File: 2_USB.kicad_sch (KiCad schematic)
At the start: 11 parts, among them J301 USB_C_Receptacle_USB2.0_16P, J302 Conn_01x03, J303 Conn_01x03, U301 CH224K, U302 FSUSB42MUX

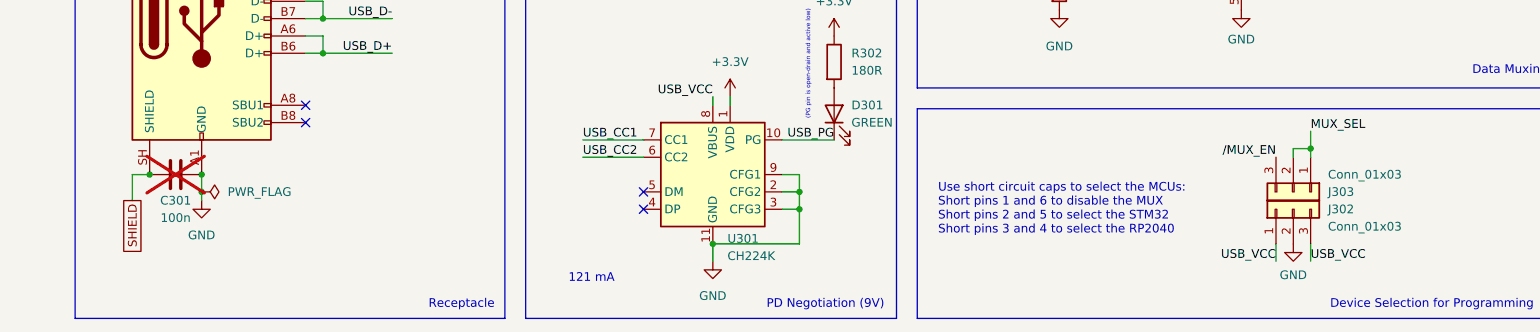
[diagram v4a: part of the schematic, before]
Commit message: Renamed a few nets
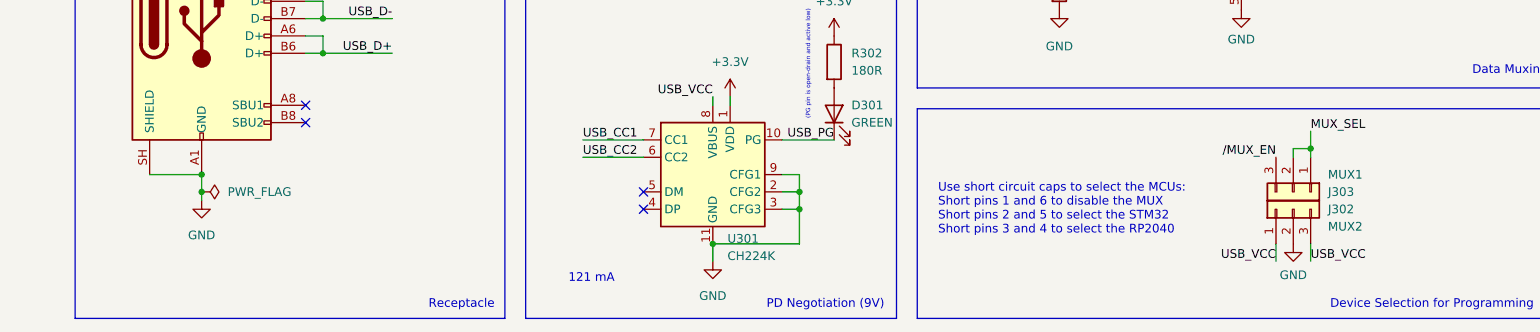
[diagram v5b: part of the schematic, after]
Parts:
- removed C301: 100n, Capacitor_SMD:C_0603_1608Metric, symbol Device:C
- J302: value Conn_01x03 -> MUX2
- J303: value Conn_01x03 -> MUX1
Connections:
- net SHIELD is gone; now on net GND: J301.SH (SHIELD)
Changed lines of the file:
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@@
 	)
 	(junction
-		(at 49.53 125.73)
+		(at 87.63 85.09)
+		(diameter 0)
+		(color 0 0 0 0)
+	)
+	(junction
+		(at 144.78 128.27)
 		(diameter 0)
 		(color 0 0 0 0)
@@
 	)
 	(junction
-		(at 87.63 85.09)
-		(diameter 0)
-		(color 0 0 0 0)
-	)
-	(junction
-		(at 144.78 128.27)
-		(diameter 0)
-		(color 0 0 0 0)
-	)
-	(junction
 		(at 85.09 85.09)
 		(diameter 0)
@@
 	(wire
 		(pts
-			(xy 46.99 129.54) (xy 46.99 125.73)
-		)
-		(stroke
-			(width 0)
-			(type default)
-		)
-	)
-	(wire
-		(pts
 			(xy 57.15 128.27) (xy 57.15 129.54)
 		)
@@
 	(wire
 		(pts
+			(xy 49.53 125.73) (xy 57.15 125.73)
+		)
+		(stroke
+			(width 0)
+			(type default)
+		)
+	)
+	(wire
+		(pts
 			(xy 132.08 114.3) (xy 132.08 115.57)
 		)
@@
 		(pts
 			(xy 144.78 128.27) (xy 144.78 130.81)
-		)
-		(stroke
-			(width 0)
-			(type default)
-		)
-	)
-	(wire
-		(pts
-			(xy 46.99 125.73) (xy 49.53 125.73)
 		)
 		(stroke
@@
 			)
 			(justify right bottom)
-		)
-	)
-	(global_label "SHIELD"
-		(shape passive)
-		(at 46.99 129.54 270)
-		(fields_autoplaced yes)
-		(effects
-			(font
-				(size 1.27 1.27)
-			)
-			(justify right)
-		)
-		(property "Intersheetrefs" "${INTERSHEET_REFS}"
-			(at 46.99 138.0058 90)
-			(hide yes)
-			(show_name no)
-			(do_not_autoplace no)
-			(effects
-				(font
-					(size 1.27 1.27)
-				)
-				(justify right)
-			)
 		)
 	)
@@
 			)
 		)
-		(property "Value" "Conn_01x03"
+		(property "Value" "MUX1"
 			(at 222.25 125.73 90)
 			(show_name no)
@@
 			)
 		)
-		(property "Value" "Conn_01x03"
+		(property "Value" "MUX2"
 			(at 222.25 133.35 90)
 			(show_name no)
@@
 					(unit 1)
 				)
-			)
-		)
-	)
-	(symbol
-		(lib_id "Device:C")
-		(at 53.34 125.73 90)
-		(unit 1)
-		(body_style 1)
-		(exclude_from_sim no)
-		(in_bom yes)
-		(on_board yes)
-		(in_pos_files yes)
-		(dnp yes)
-		(property "Reference" "C301"
-			(at 53.34 129.54 90)
-			(show_name no)
-			(do_not_autoplace no)
-			(effects
-				(font
-					(size 1.27 1.27)
-				)
-			)
-		)
-		(property "Value" "100n"
-			(at 53.34 132.08 90)
-			(show_name no)
-			(do_not_autoplace no)
-			(effects
-				(font
-					(size 1.27 1.27)
-				)
-			)
-		)
-		(property "Footprint" "Capacitor_SMD:C_0603_1608Metric"
-			(at 57.15 124.7648 0)
-			(hide yes)
-			(show_name no)
-			(do_not_autoplace no)
-			(effects
-				(font
-					(size 1.27 1.27)
-				)
-			)
-		)
-		(property "Datasheet" ""
-			(at 53.34 125.73 0)
-			(hide yes)
-			(show_name no)
-			(do_not_autoplace no)
-			(effects
-				(font
-					(size 1.27 1.27)
-				)
-			)
-		)
-		(property "Description" "Unpolarized capacitor"
-			(at 53.34 125.73 0)
-			(hide yes)
-			(show_name no)
-			(do_not_autoplace no)
-			(effects
-				(font
-					(size 1.27 1.27)
-				)
-			)
-		)
-		(property "LCSC Part Name" ""
-			(at 53.34 125.73 90)
-			(hide yes)
-			(show_name no)
-			(do_not_autoplace no)
-			(effects
-				(font
-					(size 1.27 1.27)
-				)
-			)
-		)
-		(property "Manufacturer Part" ""
-			(at 53.34 125.73 90)
-			(hide yes)
-			(show_name no)
-			(do_not_autoplace no)
-			(effects
-				(font
-					(size 1.27 1.27)
-				)
-			)
-		)
-		(property "Supplier" ""
-			(at 53.34 125.73 90)
-			(hide yes)
-			(show_name no)
-			(do_not_autoplace no)
-			(effects
-				(font
-					(size 1.27 1.27)
-				)
-			)
-		)
-		(property "Supplier Part" ""
-			(at 53.34 125.73 90)
-			(hide yes)
-			(show_name no)
-			(do_not_autoplace no)
-			(effects
-				(font
-					(size 1.27 1.27)
-				)
-			)
-		)
-		(pin "2"
-		)
-		(pin "1"
-		)
-		(instances
-			(project "polaris"
-				(path "/cfb90e19-9fbe-47a1-a5ac-df522853d1d0/f51c22fe-6c27-4a6e-b54b-9941150cfe5c"
-					(reference "C301")
-					(unit 1)
-				)

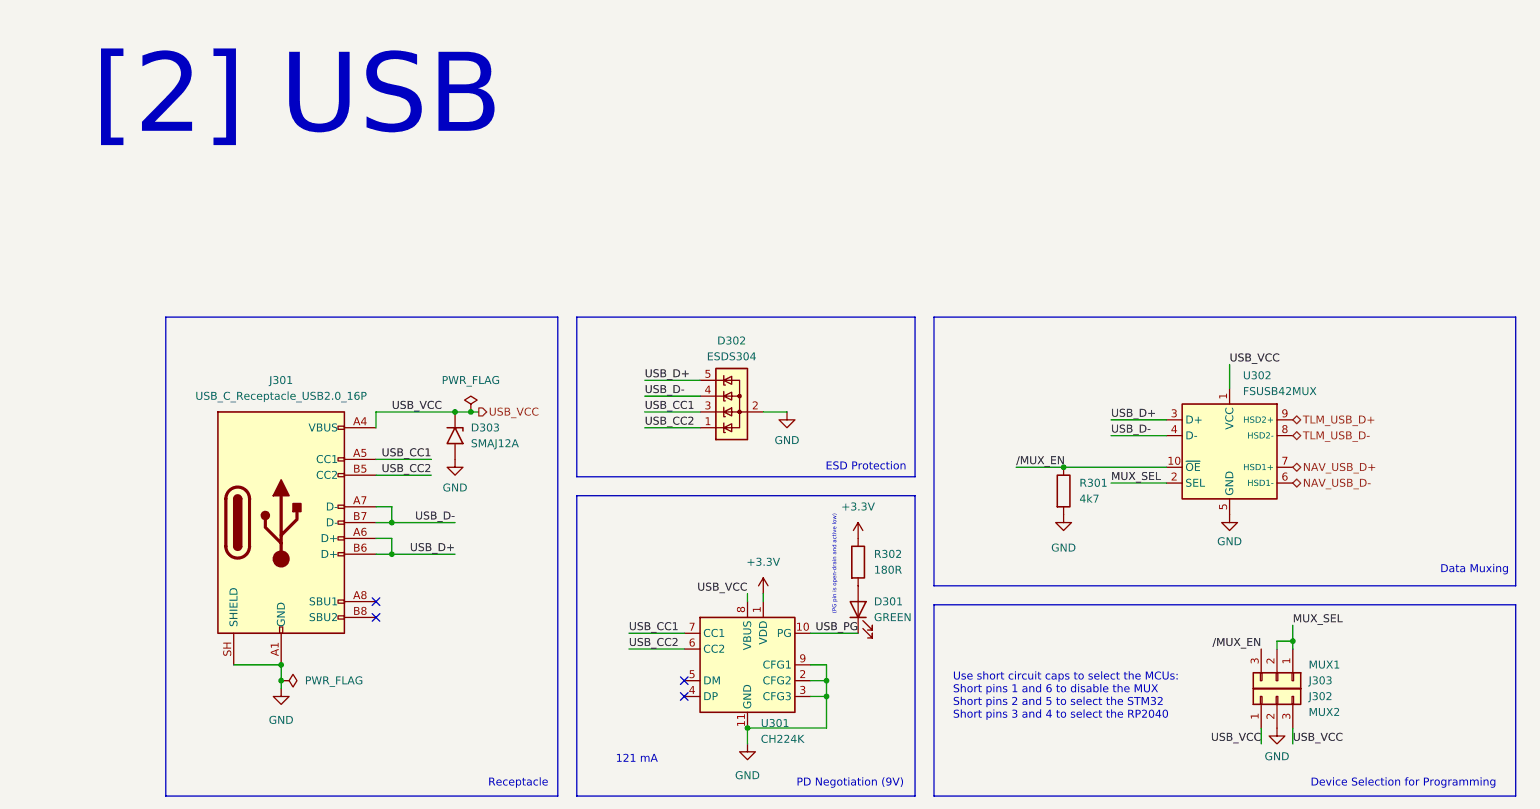
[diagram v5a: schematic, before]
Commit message: Continued ESD and USB-C section of PCB
Changed ESD device to one more suitable, previously thought unavailable
Started basic component placement
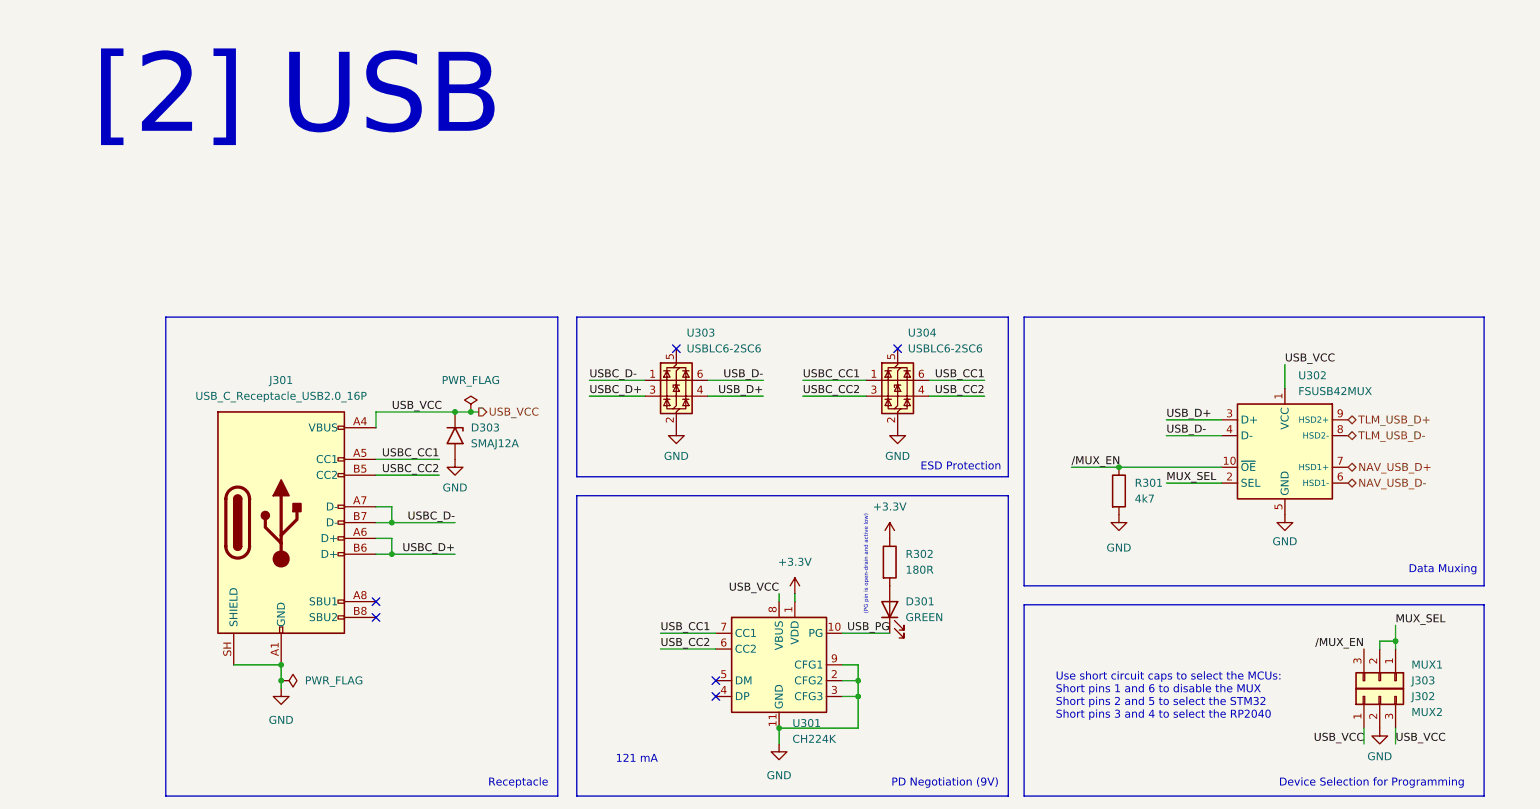
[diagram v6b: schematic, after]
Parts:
- removed D302: ESDS304, Package_TO_SOT_SMD:SOT-23-5, symbol Power_Protection:ESDS304
- added U303, U304: USBLC6-2SC6, Package_TO_SOT_SMD:SOT-23-6, symbol Power_Protection:USBLC6-2SC6
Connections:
- net GND: now also U303.2 (GND), U304.2 (GND)
- net USB_CC1: now also U304.6 (I/O1); no longer J301.A5 (CC1)
- net USB_CC2: now also U304.4 (I/O2); no longer J301.B5 (CC2)
- net USB_D+: now also U303.4 (I/O2); no longer J301.A6 (D+), J301.B6 (D+)
- net USB_D-: now also U303.6 (I/O1); no longer J301.A7 (D-), J301.B7 (D-)
- new net USBC_CC1: J301.A5 (CC1), U304.1 (I/O1)
- new net USBC_CC2: J301.B5 (CC2), U304.3 (I/O2)
- new net USBC_D+: J301.A6 (D+), J301.B6 (D+), U303.3 (I/O2)
- new net USBC_D-: J301.A7 (D-), J301.B7 (D-), U303.1 (I/O1)
- no-connect marks 4 -> 6
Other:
- moved on the sheet: D301, J302, J303, R301, R302, U301, U302

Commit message: Redesigned the whole thing for the hundredth time
Changed from dual MCU to single MCU
Changed main MCU to STM32F446VE
Added CubeMX project (ioc) file for easy access to pinouts
Note: The PCB file still contains the previous connections and footprints
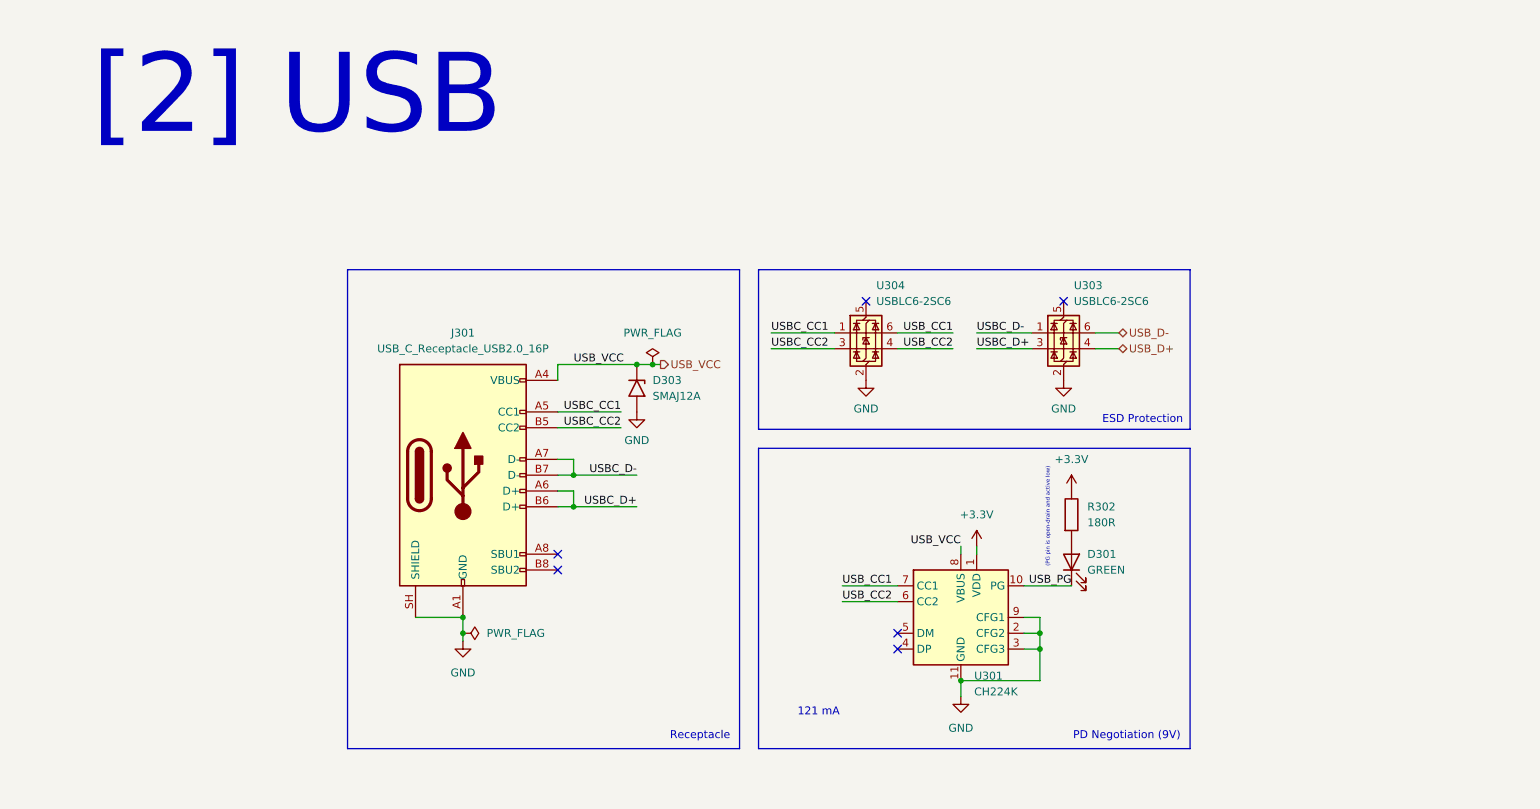
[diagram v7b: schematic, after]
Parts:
- removed J302: MUX2, Connector_PinHeader_2.54mm:PinHeader_1x03_P2.54mm_Vertical, symbol Connector_Generic:Conn_01x03
- removed J303: MUX1, Connector_PinHeader_2.54mm:PinHeader_1x03_P2.54mm_Vertical, symbol Connector_Generic:Conn_01x03
- removed R301: 4k7, Resistor_SMD:R_0603_1608Metric, symbol Device:R
- removed U302: FSUSB42MUX, Package_SO:MSOP-10_3x3mm_P0.5mm, symbol Interface_USB:FSUSB42MUX
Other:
- note removed: "Data Muxing"
- note removed: "Device Selection for Programming"
- note removed: "Use short circuit caps to select the MCUs: Short pins 1 and 6 to disable the MUX Short pins 2 and 5 to select the STM32 Short pins 3 and 4 to select the RP2040"
- moved on the sheet: D301, D303, J301, R302, U301, U303, U304
